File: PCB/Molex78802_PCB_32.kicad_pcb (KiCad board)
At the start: 2 copper layers, 16.6 x 43.1 mm, 1 part

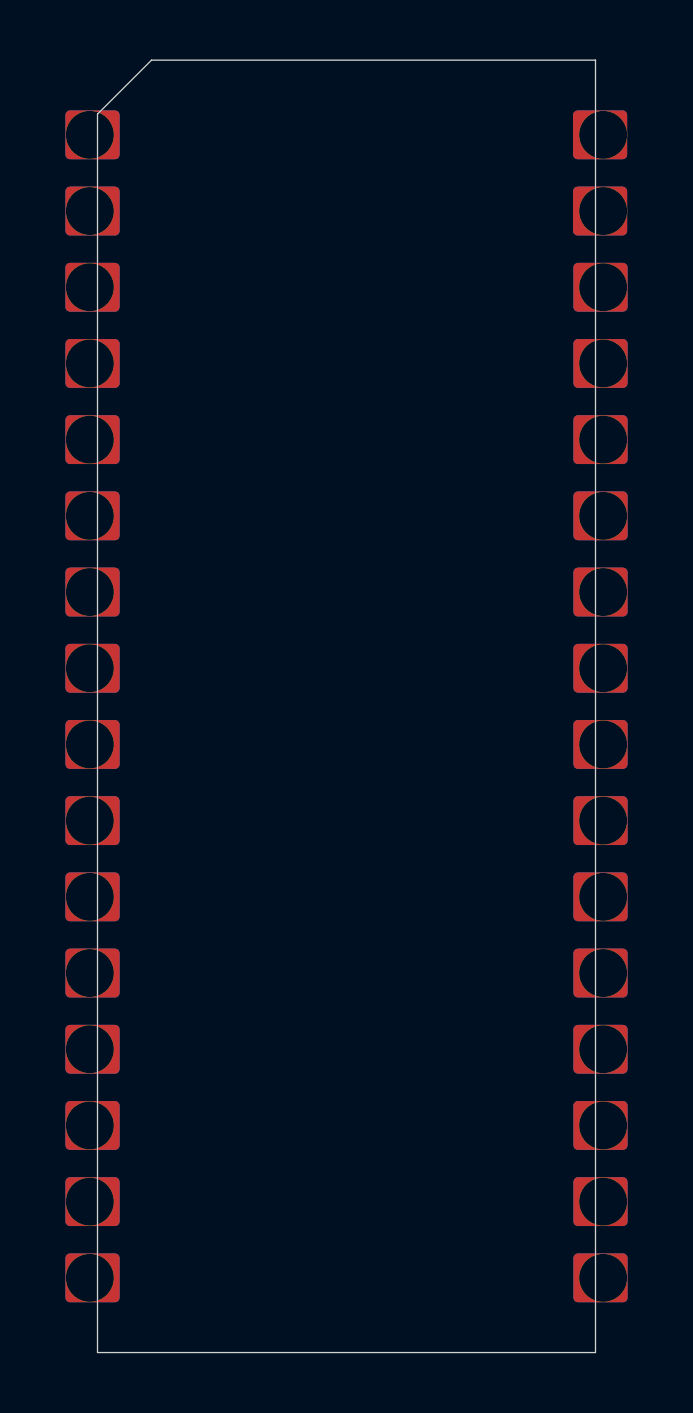
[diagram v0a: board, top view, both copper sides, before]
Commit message: kicad v6, better castellated pads, add slotted version
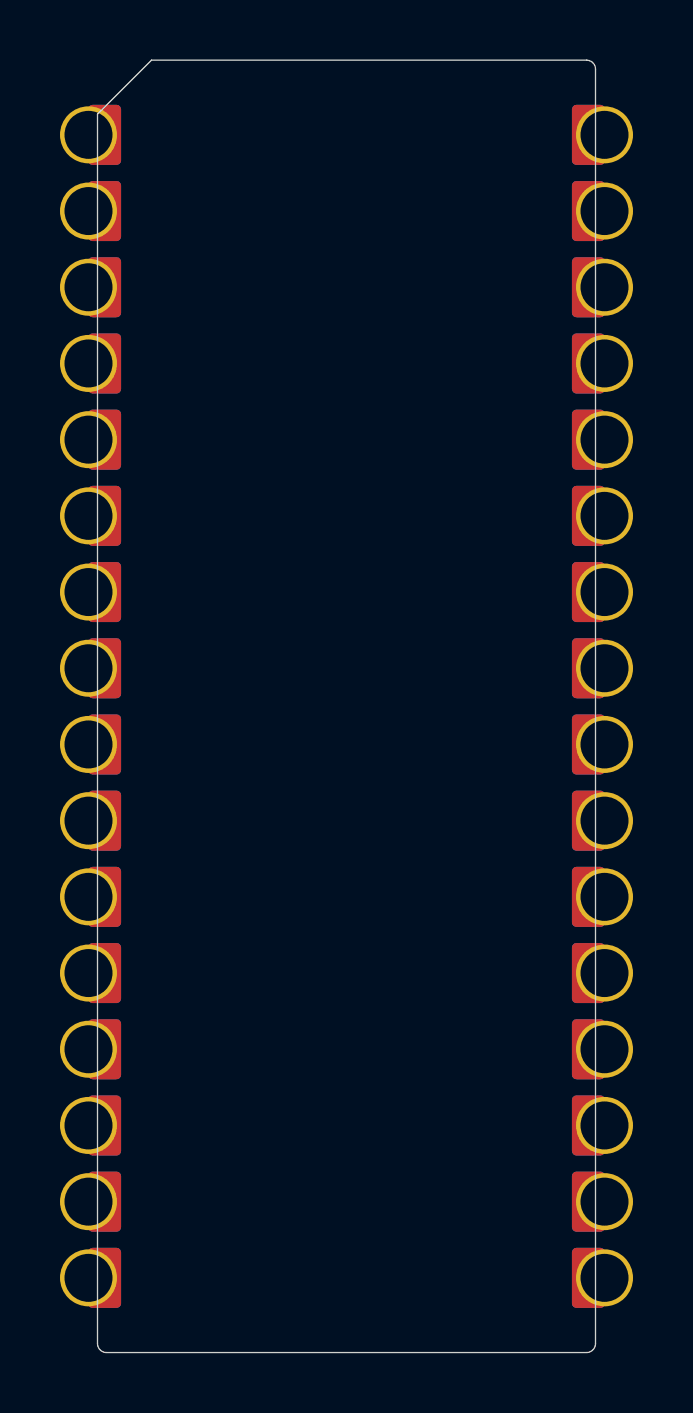
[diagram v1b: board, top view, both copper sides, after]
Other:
- outline, holes or cut-outs redrawn
- net class Default removed
